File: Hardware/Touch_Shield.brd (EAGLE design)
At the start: 53.3 x 59.7 mm, 17 parts, among them IC1 MPR121, Q1 BSS138, Q2 BSS138, U1 ARDUINO_SHIELDLABEL

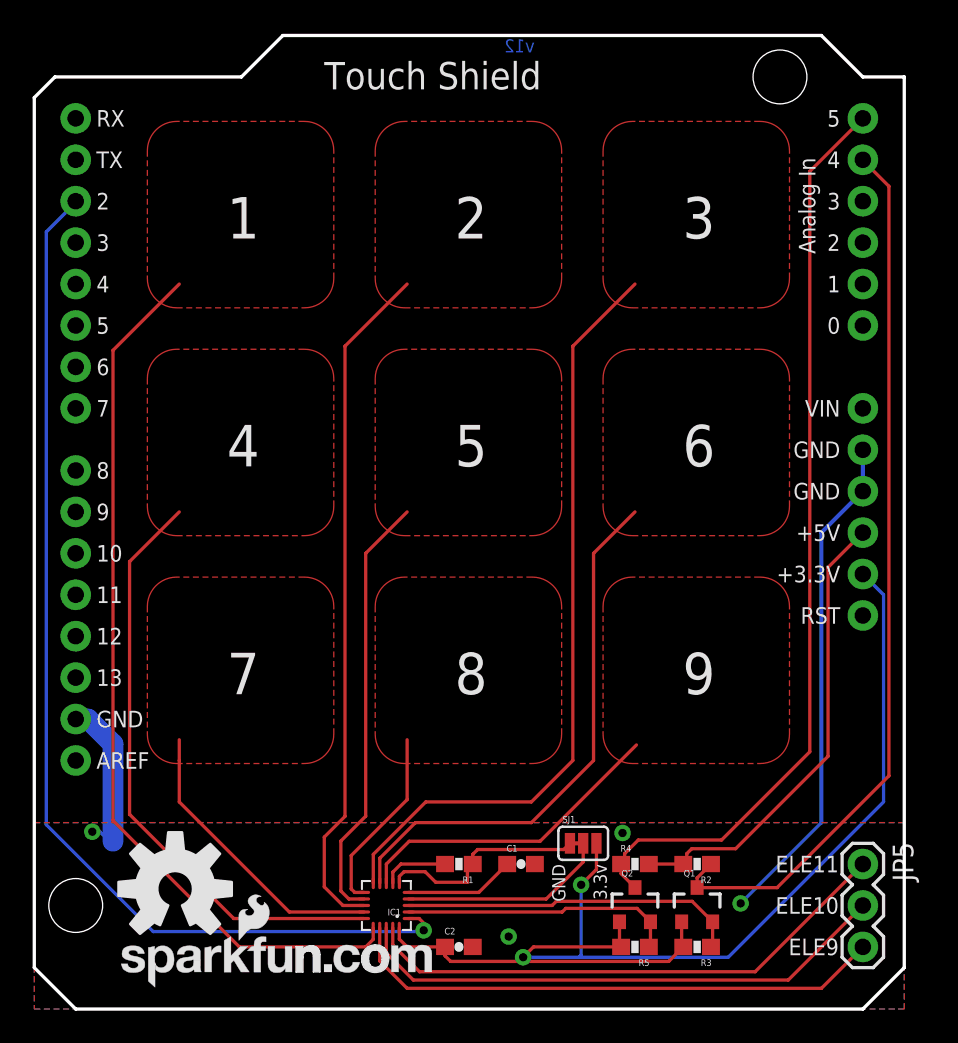
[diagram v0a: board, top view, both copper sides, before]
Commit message: Updating shield layout to R3
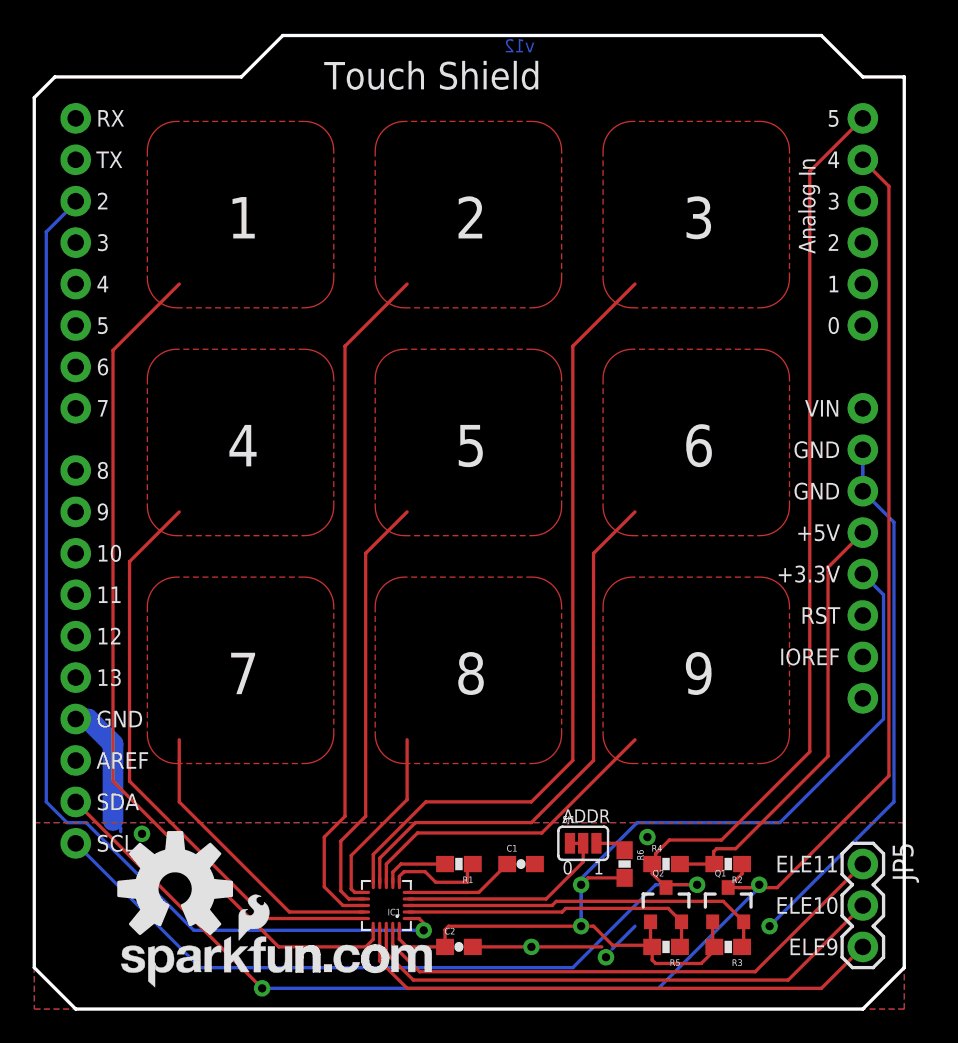
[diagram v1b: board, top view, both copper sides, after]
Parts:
- added R6: 10K, SparkFun-Resistors:0603-RES
- U1: value ARDUINO_SHIELDLABEL -> ARDUINO_R3_SHIELD; device SparkFun:DUEMILANOVE_SHIELD -> SparkFun-Boards:UNO_R3_SHIELD
- moved Q1 1.91 mm to (42.5, 6.35)
- moved Q2 1.91 mm to (38.7, 6.35)
- moved R2 1.91 mm to (42.5, 8.89)
- moved R3 1.91 mm to (42.5, 3.81)
- moved R4 1.91 mm to (38.7, 8.89)
- moved R5 1.91 mm to (38.7, 3.81)
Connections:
- new net IOREF: U1.IOREF
- new net N$2: R6.1, SJ1.3
- net 3.3V: now also R6.2; no longer SJ1.3
- net SCL_H: now also U1.SCL
- net SDA_H: now also U1.SDA
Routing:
- net SDA_H: track 54.8 -> 103.8 mm, vias 0 -> 2
- net SCL_H: track 56.6 -> 100.1 mm, vias 0 -> 1
- net 3.3V: track 77.5 -> 64.4 mm
- net GND: track 54.9 -> 58.6 mm, vias 4 -> 5
- net SCL_L: track 16.8 -> 18.7 mm
- net SDA_L: track 20.8 -> 22.7 mm
- net N$2: track 0.00 -> 1.90 mm
- net 5V: track 28.6 -> 26.9 mm
- net PAD1: track 54.6 -> 53.2 mm
- net PAD4: track 36.8 -> 35.6 mm
- net *IRQ: track 66.4 -> 65.5 mm
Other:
- board text added: "0"
- board text added: "ADDR"
- board text removed: "3.3v"
- board text removed: "GND"

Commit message: Updating all the resistors to the same production ID number
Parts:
- R2, R3, R4, R5: device SparkFun:0603-RES -> SparkFun-Resistors:0603-RES
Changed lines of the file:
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@@
 <setting verticaltext="up"/>
 </settings>
-<grid distance="0.025" unitdist="inch" unit="inch" style="lines" multiple="1" display="yes" altdistance="0.005" altunitdist="inch" altunit="inch"/>
+<grid distance="0.05" unitdist="inch" unit="inch" style="lines" multiple="1" display="yes" altdistance="0.005" altunitdist="inch" altunit="inch"/>
 <layers>
 <layer number="1" name="Top" color="4" fill="1" visible="yes" active="yes"/>
@@
 <element name="U1" library="SparkFun-Boards" package="UNO_R3_SHIELD" value="ARDUINO_R3_SHIELD" x="0" y="0"/>
 <element name="JP5" library="SparkFun" package="1X03" value="extra" x="50.8" y="8.89" rot="R270"/>
-<element name="R2" library="SparkFun" package="0603-RES" value="10k" x="42.545" y="8.89" rot="R180"/>
+<element name="R2" library="SparkFun-Resistors" package="0603-RES" value="10k" x="42.545" y="8.89" rot="R180">
+<attribute name="PROD_ID" value="RES-00824" x="42.545" y="8.89" size="1.778" layer="27" rot="R180" display="off"/>
+<attribute name="VALUE" value="10K" x="42.545" y="8.89" size="1.778" layer="27" rot="R180" display="off"/>
+</element>
 <element name="Q1" library="SparkFun" package="SOT23-3" value="BSS138" x="42.545" y="6.35"/>
-<element name="R4" library="SparkFun" package="0603-RES" value="10k" x="38.735" y="8.89"/>
+<element name="R4" library="SparkFun-Resistors" package="0603-RES" value="10k" x="38.735" y="8.89">
+<attribute name="PROD_ID" value="RES-00824" x="38.735" y="8.89" size="1.778" layer="27" display="off"/>
+<attribute name="VALUE" value="10K" x="38.735" y="8.89" size="1.778" layer="27" display="off"/>
+</element>
 <element name="Q2" library="SparkFun" package="SOT23-3" value="BSS138" x="38.735" y="6.35"/>
-<element name="R3" library="SparkFun" package="0603-RES" value="10k" x="42.545" y="3.81" rot="R180"/>
-<element name="R5" library="SparkFun" package="0603-RES" value="10k" x="38.735" y="3.81" rot="R180"/>
+<element name="R3" library="SparkFun-Resistors" package="0603-RES" value="10k" x="42.545" y="3.81" rot="R180">
+<attribute name="PROD_ID" value="RES-00824" x="42.545" y="3.81" size="1.778" layer="27" rot="R180" display="off"/>
+<attribute name="VALUE" value="10K" x="42.545" y="3.81" size="1.778" layer="27" rot="R180" display="off"/>
+</element>
+<element name="R5" library="SparkFun-Resistors" package="0603-RES" value="10k" x="38.735" y="3.81" rot="R180">
+<attribute name="PROD_ID" value="RES-00824" x="38.735" y="3.81" size="1.778" layer="27" rot="R180" display="off"/>
+<attribute name="VALUE" value="10K" x="38.735" y="3.81" size="1.778" layer="27" rot="R180" display="off"/>
+</element>
 <element name="U$5" library="SparkFun-Aesthetics" package="OSHW-LOGO-L" value="OSHW-LOGOL" x="8.636" y="7.366"/>
 <element name="FRAME1" library="SparkFun-Aesthetics" package="CREATIVE_COMMONS" value="FRAME-LETTER" x="-4.34045625" y="-22.86"/>
@@
 </signal>
 </signals>
-<errors>
-</errors>
 </board>
 </drawing>

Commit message: Re-panelized and added fiducials to board
I re-did the panel to 4 boards and added local fiducials
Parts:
- added FID1, FID2: FIDUCIALUFIDUCIAL, SparkFun-Aesthetics:MICRO-FIDUCIAL
